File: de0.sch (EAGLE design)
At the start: 149 parts, among them IC1 PL2303SA__LF, J2 UX60SC-MB-5ST, Q1 AS9013-H-HF, Q2 AS9013-H-HF, Q3 AS9013-H-HF, Q4 AS9013-H-HF, Q5 AS9013-H-HF, SW0 SS12SDP2, SW1 SS12SDP2, SW2 SS12SDP2, SW3 SS12SDP2, U1 P0082, U2 RFM95W-915S2, U3 TPS76201DBVR, U4 TPS76201DBVR, U5 TPS76201DBVR

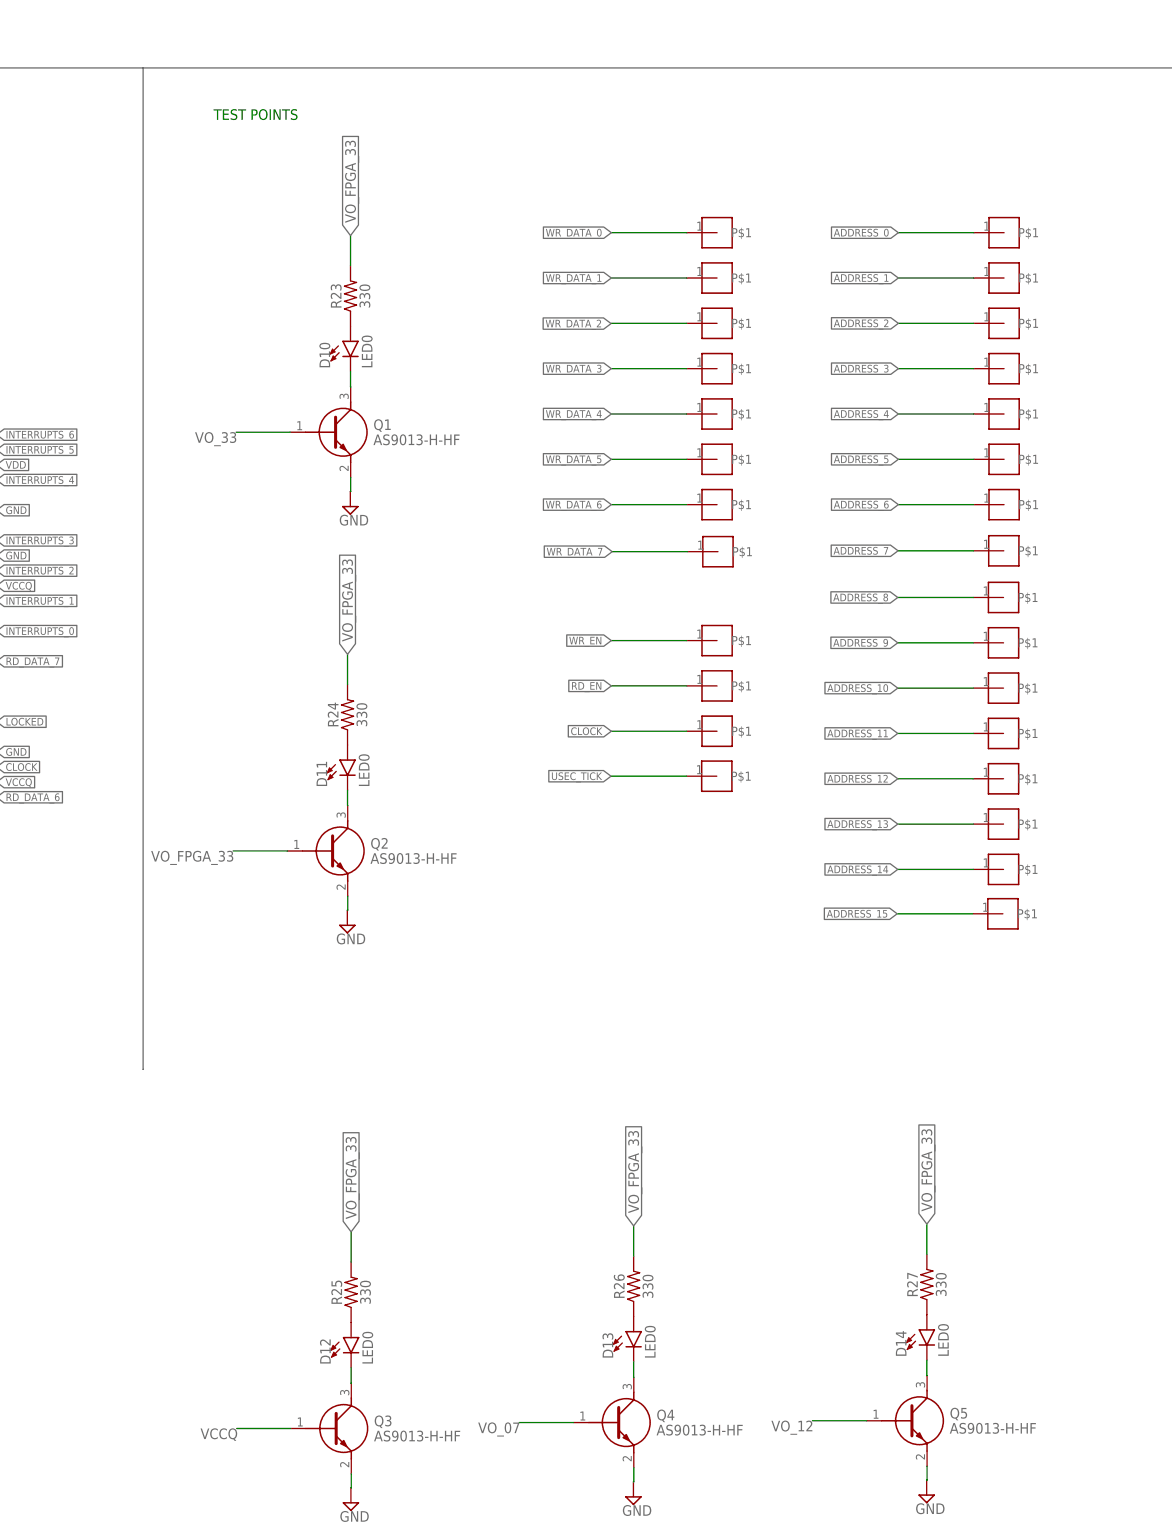
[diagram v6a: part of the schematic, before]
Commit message: change BJT to MOSFET for power leds
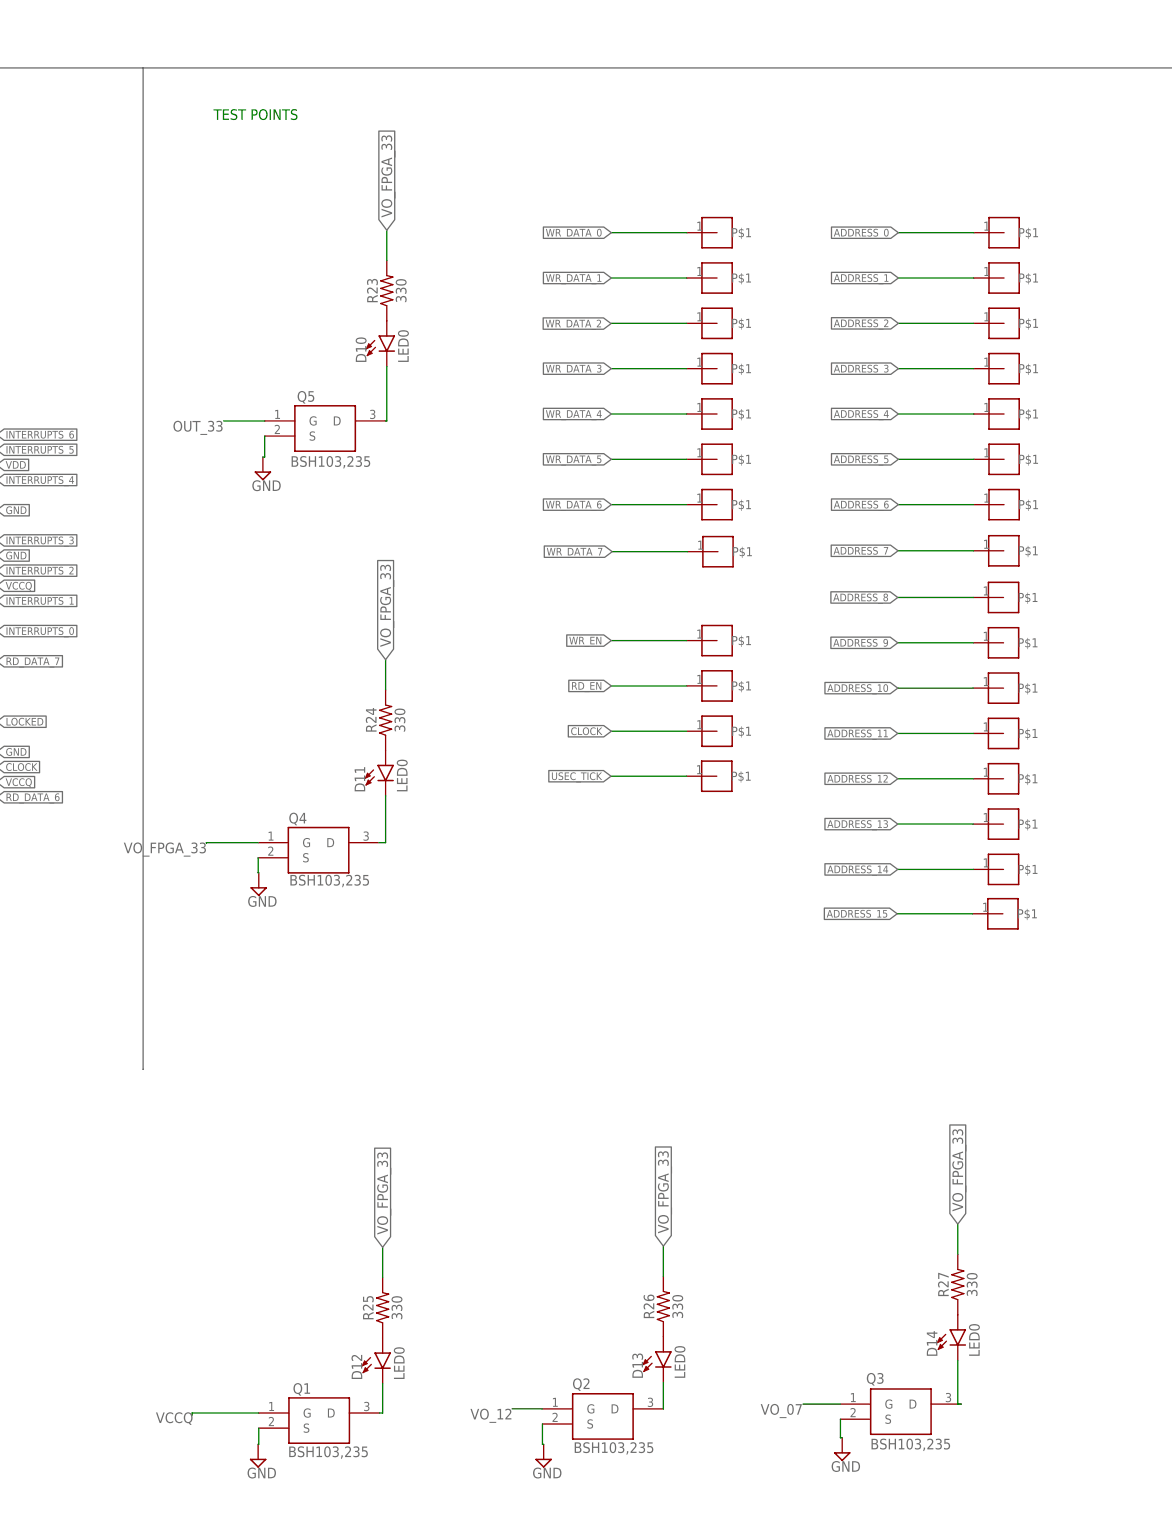
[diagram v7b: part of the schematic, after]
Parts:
- Q1, Q2, Q3, Q4, Q5: value AS9013-H-HF -> BSH103,235; device SamacSys_Parts:AS9013-H-HF -> SamacSys_Parts:BSH103,235
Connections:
- net GND: now also Q1.S, Q2.S, Q3.S, Q4.S, Q5.S; no longer Q1.E, Q2.E, Q3.E, Q4.E, Q5.E
- net N$10: now also Q5.D; no longer Q1.C
- net N$12: now also Q4.D; no longer Q2.C
- net N$14: now also Q1.D; no longer Q3.C
- net N$16: now also Q2.D; no longer Q4.C
- net N$19: now also Q3.D; no longer Q5.C
- net OUT_33: now also Q5.G
- net VCCQ: now also Q1.G; no longer Q3.B
- net VO_07: now also Q3.G; no longer Q4.B
- net VO_12: now also Q2.G; no longer Q5.B
- net VO_33: no longer Q1.B
- net VO_FPGA_33: now also Q4.G; no longer Q2.B
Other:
- moved on the sheet: D10, D11, D12, D13, D14, R23, R24, R25, R26, R27

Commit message: Update again with Duran's suggest
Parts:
- removed JP1, JP2, JP3: (no value), jumper:JP1Q
- added H1, H2, H3, H4: MOUNT-HOLE3.3, holes:MOUNT-HOLE3.3
- added J1: (no value), SparkFun-Connectors:CONN_02
- added LORA_DIO0, LORA_NSS, LORA_RESET: (no value), jumper:JP1Q
- renumbered 5V_JUMPER to 5V, REG_IN_07 to IN_07, REG_IN_12 to IN_12, REG_IN_33 to IN_33, REG_OUT_07 to OUT_07, REG_OUT_12 to OUT_12, REG_OUT_33 to OUT_33, UART_JUMPER to UART
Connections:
- net LOCKED: now also J1.1
- net LORA_DIO0: now also LORA_DIO0.1; no longer JP1.1
- net LORA_NSS: now also LORA_NSS.1; no longer JP3.1
- net LORA_RESET: now also LORA_RESET.1; no longer JP2.1
- net N$10: now also Q1.D; no longer Q5.D
- net N$12: now also D12.C, Q3.D; no longer D11.C, Q4.D
- net N$14: now also D11.C, Q2.D; no longer D12.C, Q1.D
- net N$16: now also Q4.D; no longer Q2.D
- net N$19: now also Q5.D; no longer Q3.D
- net N$23: now also LORA_DIO0.2; no longer JP1.2
- net N$24: now also LORA_RESET.2; no longer JP2.2
- net N$25: now also LORA_NSS.2; no longer JP3.2
- net OUT_33: now also Q1.G; no longer Q5.G
- net RESET: now also J1.2
- net VCCQ: no longer Q1.G
- net VO_07: now also Q5.G; no longer Q3.G
- net VO_12: now also Q4.G; no longer Q2.G
- net VO_33: now also Q2.G, R23.2, R24.2, R25.2, R26.2, R27.2
- net VO_FPGA_33: now also Q3.G; no longer Q4.G, R23.2, R24.2, R25.2, R26.2, R27.2
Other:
- note added: "Mounting holes"
- note added: "Power leds"
- moved on the sheet: D1, D10, D11, D12, D13, D14, D2, D3, D4, D5, D6, D7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
